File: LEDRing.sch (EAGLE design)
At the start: 35 parts, among them U1 ATMEGA328P-AU, U2 MCP73831, U3 MIC5219 3.3V, U4 MMA8452Q, Y1 16MHZ

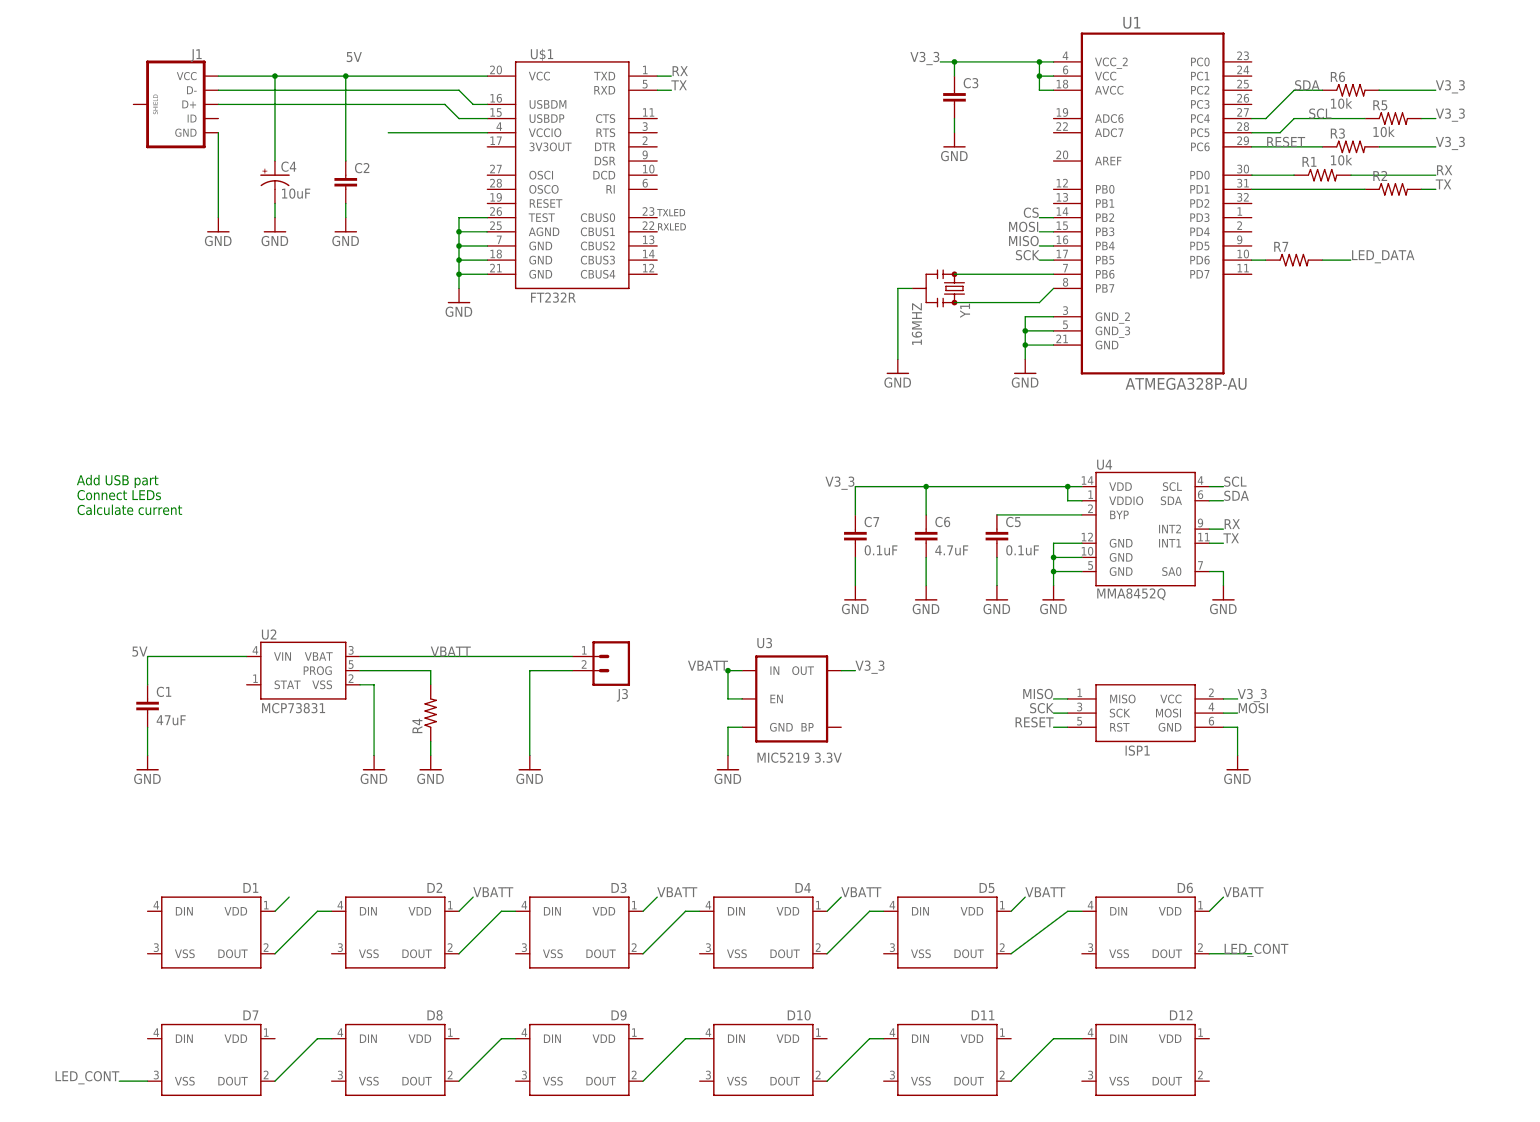
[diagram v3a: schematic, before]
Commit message: Moved USB connector
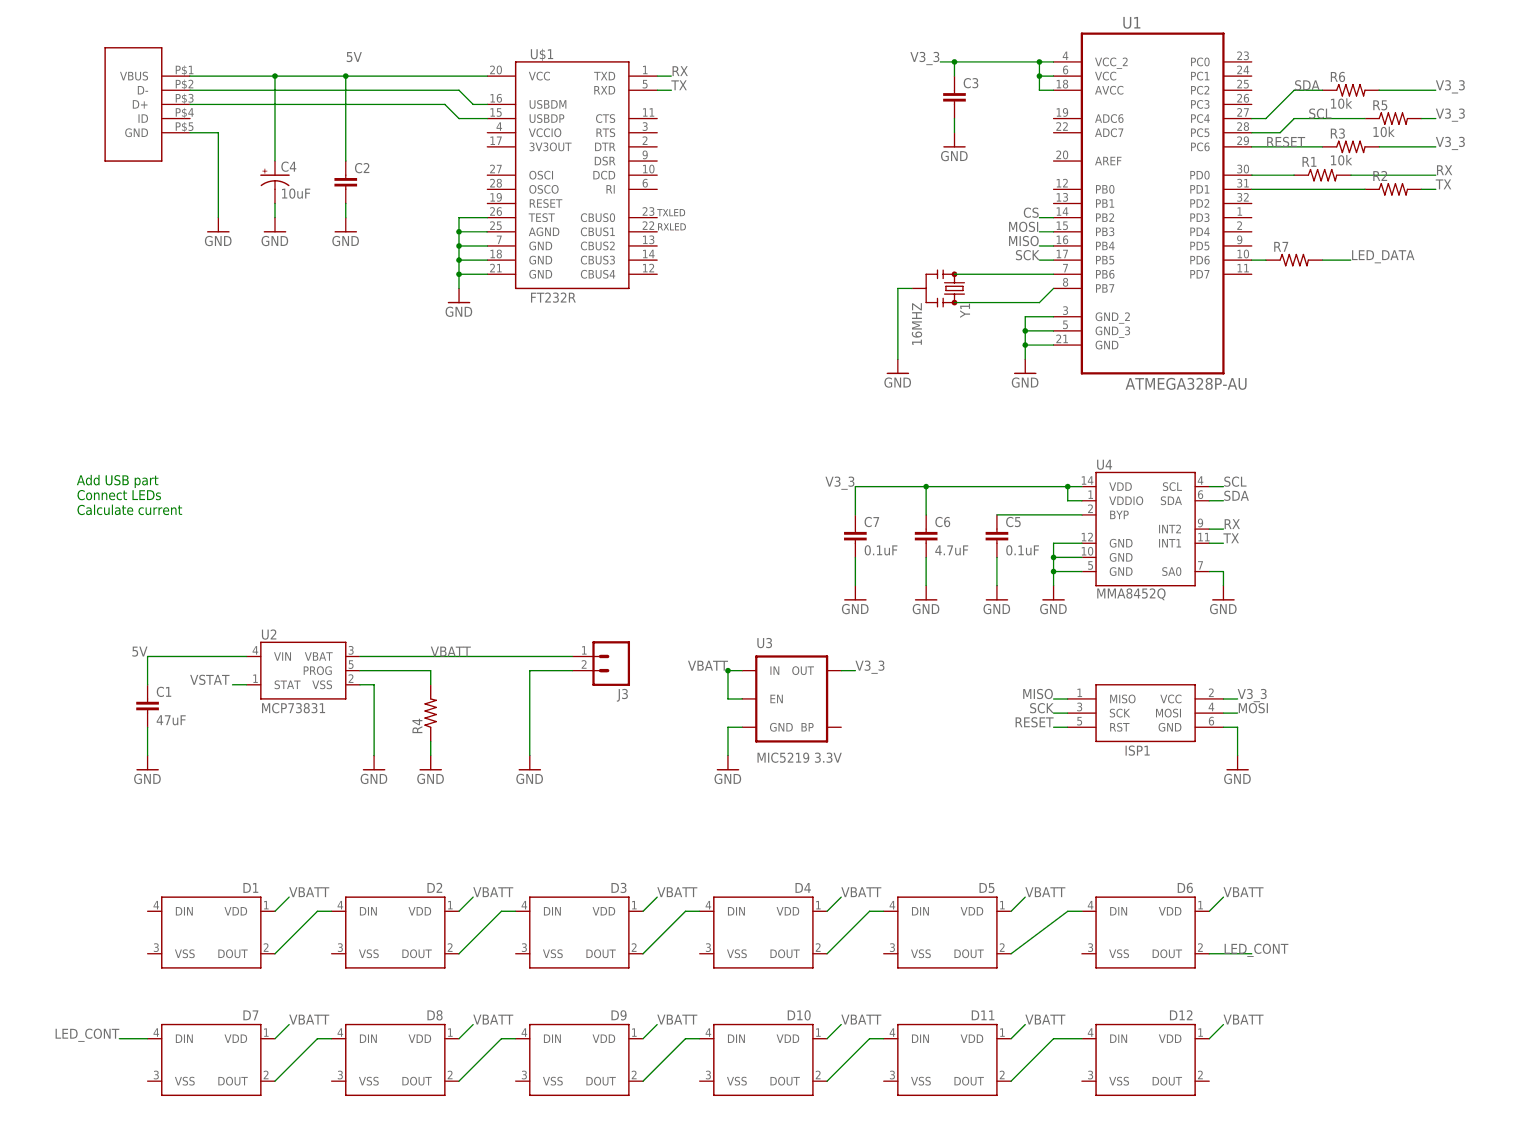
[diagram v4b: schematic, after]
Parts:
- removed J1: (no value), SparkFun-Connectors:USB_MICROB_PLUG-SMT
- added U$2: TE_USB_A121025CT, LEDRingLib:TE_USB_A121025CT
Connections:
- removed net N$6: U$1.VCCIO
- new net VSTAT: U2.STAT
- net 5V: now also U$2.VBUS; no longer J1.VCC
- net GND: now also U$2.GND; no longer J1.GND
- net LED_CONT: now also D7.DIN; no longer D7.VSS
- net N$4: now also U$2.D-; no longer J1.D-
- net N$5: now also U$2.D+; no longer J1.D+
- net VBATT: now also D10.VDD, D11.VDD, D12.VDD, D7.VDD, D8.VDD, D9.VDD
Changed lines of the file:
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@@
 <part name="R2" library="SparkFun-Passives" deviceset="RESISTOR" device="0603-RES"/>
 <part name="U$1" library="GeekAmmo" deviceset="FT232R" device=""/>
-<part name="J1" library="SparkFun-Connectors" deviceset="USB_MICROB_PLUG" device="-SMT"/>
 <part name="GND1" library="SparkFun-Aesthetics" deviceset="GND" device=""/>
 <part name="GND2" library="SparkFun-Aesthetics" deviceset="GND" device=""/>
@@
 <part name="D12" library="SparkFun-LED" deviceset="WS2812B" device=""/>
 <part name="J3" library="SparkFun-Connectors" deviceset="M02" device="PTH"/>
+<part name="U$2" library="LEDRingLib" deviceset="TE_USB_A121025CT" device=""/>
 </parts>
 <sheets>
@@
 <instance part="R2" gate="G$1" x="137.16" y="73.66"/>
 <instance part="U$1" gate="G$1" x="-10.16" y="76.2"/>
-<instance part="J1" gate="G$1" x="-81.28" y="88.9" rot="MR0"/>
 <instance part="GND1" gate="1" x="-73.66" y="66.04"/>
 <instance part="GND2" gate="1" x="-63.5" y="66.04"/>
@@
 <instance part="D12" gate="G$1" x="99.06" y="-83.82" rot="MR0"/>
 <instance part="J3" gate="G$1" x="-2.54" y="-10.16" rot="R180"/>
+<instance part="U$2" gate="G$1" x="-88.9" y="88.9"/>
 </instances>
 <busses>
@@
 <net name="5V" class="0">
 <segment>
-<pinref part="J1" gate="G$1" pin="VCC"/>
 <pinref part="U$1" gate="G$1" pin="VCC"/>
-<wire x1="-73.66" y1="93.98" x2="-63.5" y2="93.98" width="0.1524" layer="91"/>
+<wire x1="-78.74" y1="93.98" x2="-63.5" y2="93.98" width="0.1524" layer="91"/>
 <wire x1="-63.5" y1="93.98" x2="-50.8" y2="93.98" width="0.1524" layer="91"/>
 <wire x1="-50.8" y1="93.98" x2="-25.4" y2="93.98" width="0.1524" layer="91"/>
@@
 <pinref part="C4" gate="G$1" pin="+"/>
 <label x="-50.8" y="96.52" size="1.778" layer="95"/>
+<pinref part="U$2" gate="G$1" pin="VBUS"/>
 </segment>
 <segment>
@@
 <net name="N$4" class="0">
 <segment>
-<pinref part="J1" gate="G$1" pin="D-"/>
-<wire x1="-73.66" y1="91.44" x2="-30.48" y2="91.44" width="0.1524" layer="91"/>
+<wire x1="-78.74" y1="91.44" x2="-30.48" y2="91.44" width="0.1524" layer="91"/>
 <wire x1="-30.48" y1="91.44" x2="-27.94" y2="88.9" width="0.1524" layer="91"/>
 <pinref part="U$1" gate="G$1" pin="USBDM"/>
 <wire x1="-27.94" y1="88.9" x2="-25.4" y2="88.9" width="0.1524" layer="91"/>
+<pinref part="U$2" gate="G$1" pin="D-"/>
 </segment>
 </net>
 <net name="N$5" class="0">
 <segment>
-<pinref part="J1" gate="G$1" pin="D+"/>
-<wire x1="-73.66" y1="88.9" x2="-33.02" y2="88.9" width="0.1524" layer="91"/>
+<wire x1="-78.74" y1="88.9" x2="-33.02" y2="88.9" width="0.1524" layer="91"/>
 <wire x1="-33.02" y1="88.9" x2="-30.48" y2="86.36" width="0.1524" layer="91"/>
 <pinref part="U$1" gate="G$1" pin="USBDP"/>
 <wire x1="-30.48" y1="86.36" x2="-25.4" y2="86.36" width="0.1524" layer="91"/>
+<pinref part="U$2" gate="G$1" pin="D+"/>
 </segment>
 </net>
 <net name="GND" class="0">
 <segment>
-<pinref part="J1" gate="G$1" pin="GND"/>
 <pinref part="GND1" gate="1" pin="GND"/>
 <wire x1="-73.66" y1="83.82" x2="-73.66" y2="68.58" width="0.1524" layer="91"/>
+<pinref part="U$2" gate="G$1" pin="GND"/>
+<wire x1="-78.74" y1="83.82" x2="-73.66" y2="83.82" width="0.1524" layer="91"/>
 </segment>
 <segment>
@@
 </segment>
 </net>
-<net name="N$6" class="0">
-<segment>
-<pinref part="U$1" gate="G$1" pin="VCCIO"/>
-<wire x1="-25.4" y1="83.82" x2="-43.18" y2="83.82" width="0.1524" layer="91"/>
-</segment>
-</net>
 <net name="N$7" class="0">
 <segment>
@@
 <pinref part="D1" gate="G$1" pin="VDD"/>
 <wire x1="-63.5" y1="-55.88" x2="-60.96" y2="-53.34" width="0.1524" layer="91"/>
+<label x="-60.96" y="-53.34" size="1.778" layer="95"/>
 </segment>
 <segment>
@@
 <wire x1="104.14" y1="-55.88" x2="106.68" y2="-53.34" width="0.1524" layer="91"/>
 <label x="106.68" y="-53.34" size="1.778" layer="95"/>
+</segment>
+<segment>
+<pinref part="D7" gate="G$1" pin="VDD"/>
+<wire x1="-63.5" y1="-78.74" x2="-60.96" y2="-76.2" width="0.1524" layer="91"/>
+<label x="-60.96" y="-76.2" size="1.778" layer="95"/>
+</segment>
+<segment>
+<pinref part="D8" gate="G$1" pin="VDD"/>
+<wire x1="-30.48" y1="-78.74" x2="-27.94" y2="-76.2" width="0.1524" layer="91"/>
+<label x="-27.94" y="-76.2" size="1.778" layer="95"/>
+</segment>
+<segment>
+<pinref part="D9" gate="G$1" pin="VDD"/>
+<wire x1="2.54" y1="-78.74" x2="5.08" y2="-76.2" width="0.1524" layer="91"/>
+<label x="5.08" y="-76.2" size="1.778" layer="95"/>
+</segment>
+<segment>
+<pinref part="D10" gate="G$1" pin="VDD"/>
+<wire x1="35.56" y1="-78.74" x2="38.1" y2="-76.2" width="0.1524" layer="91"/>
+<label x="38.1" y="-76.2" size="1.778" layer="95"/>
+</segment>
+<segment>
+<pinref part="D11" gate="G$1" pin="VDD"/>
+<wire x1="68.58" y1="-78.74" x2="71.12" y2="-76.2" width="0.1524" layer="91"/>
+<label x="71.12" y="-76.2" size="1.778" layer="95"/>
+</segment>
+<segment>
+<pinref part="D12" gate="G$1" pin="VDD"/>
+<wire x1="104.14" y1="-78.74" x2="106.68" y2="-76.2" width="0.1524" layer="91"/>
+<label x="106.68" y="-76.2" size="1.778" layer="95"/>
 </segment>
 </net>
@@
 </segment>
 <segment>
-<pinref part="D7" gate="G$1" pin="VSS"/>
-<wire x1="-86.36" y1="-86.36" x2="-91.44" y2="-86.36" width="0.1524" layer="91"/>
-<label x="-91.44" y="-86.36" size="1.778" layer="95" rot="MR0"/>
+<pinref part="D7" gate="G$1" pin="DIN"/>
+<wire x1="-86.36" y1="-78.74" x2="-91.44" y2="-78.74" width="0.1524" layer="91"/>
+<label x="-91.44" y="-78.74" size="1.778" layer="95" rot="MR0"/>
 </segment>
 </net>
@@
 </segment>
 </net>
+<net name="VSTAT" class="0">
+<segment>
+<pinref part="U2" gate="G$1" pin="STAT"/>
+<wire x1="-68.58" y1="-15.24" x2="-71.12" y2="-15.24" width="0.1524" layer="91"/>
+<label x="-78.74" y="-15.24" size="1.778" layer="95"/>
+</segment>
+</net>

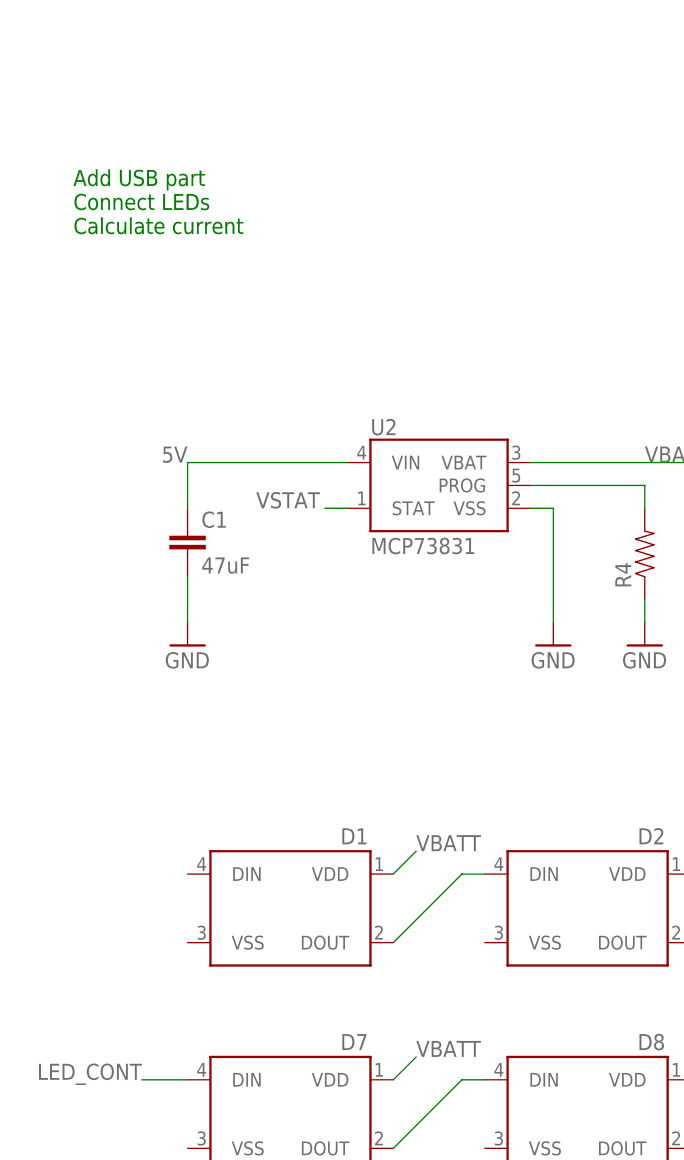
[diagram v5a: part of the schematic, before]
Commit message: Started tieing LED VSS to GND
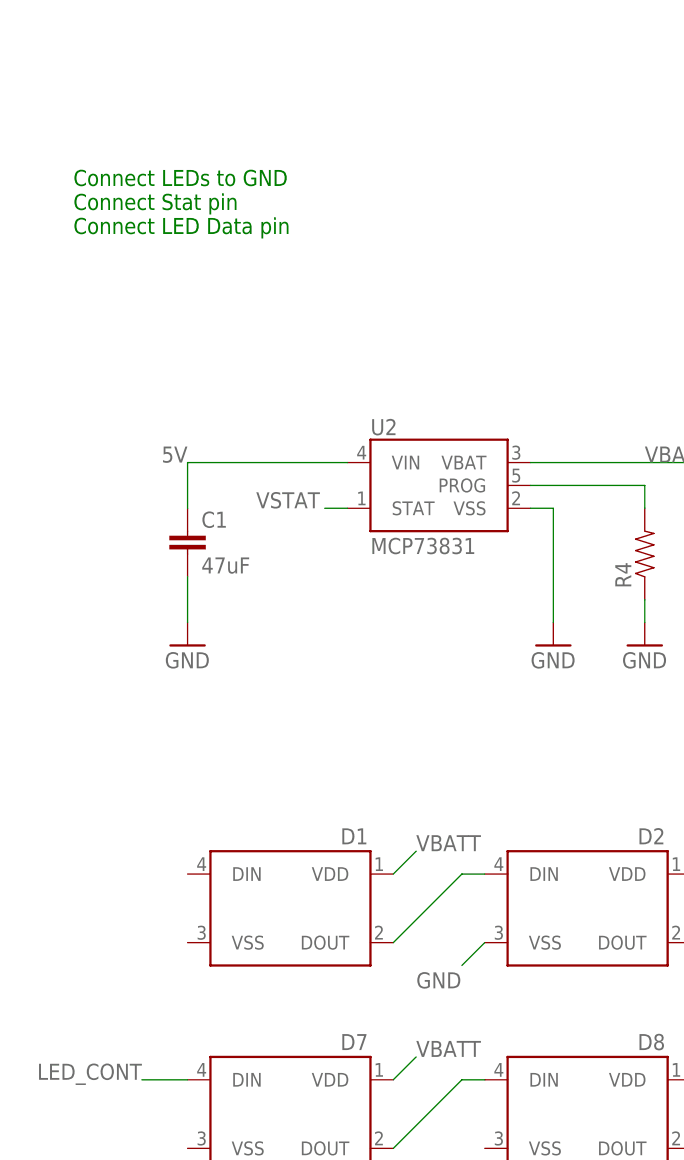
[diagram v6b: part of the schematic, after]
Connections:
- net GND: now also D2.VSS
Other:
- note added: "Connect LEDs to GND Connect Stat pin Connect LED Data pin"
- note removed: "Add USB part Connect LEDs Calculate current"
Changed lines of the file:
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@@
 <sheet>
 <plain>
-<text x="-99.06" y="15.24" size="1.778" layer="91">Add USB part
-Connect LEDs
-Calculate current
-</text>
+<text x="-99.06" y="15.24" size="1.778" layer="91">Connect LEDs to GND
+Connect Stat pin
+Connect LED Data pin</text>
 </plain>
 <instances>
@@
 <wire x1="53.34" y1="7.62" x2="53.34" y2="2.54" width="0.1524" layer="91"/>
 </segment>
-</net>
+<segment>
+<pinref part="D2" gate="G$1" pin="VSS"/>
+<wire x1="-53.34" y1="-63.5" x2="-55.88" y2="-66.04" width="0.1524" layer="91"/>
+<label x="-60.96" y="-68.58" size="1.778" layer="95"/>
+</segment>
+</net>

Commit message: Finished layout. Need to fix text
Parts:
- added R8: (no value), SparkFun-Passives:RESISTOR0603-RES
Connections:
- net 5V: now also R8.2
- net GND: now also D1.VSS, D10.VSS, D11.VSS, D12.VSS, D3.VSS, D4.VSS, D5.VSS, D6.VSS, D7.VSS, D8.VSS, D9.VSS
- net LED_DATA: now also D1.DIN
- net VSTAT: now also R8.1, U1.PD3
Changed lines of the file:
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@@
 <part name="J3" library="SparkFun-Connectors" deviceset="M02" device="PTH"/>
 <part name="U$2" library="LEDRingLib" deviceset="TE_USB_A121025CT" device=""/>
+<part name="R8" library="SparkFun-Passives" deviceset="RESISTOR" device="0603-RES"/>
 </parts>
 <sheets>
@@
 <instance part="J3" gate="G$1" x="-2.54" y="-10.16" rot="R180"/>
 <instance part="U$2" gate="G$1" x="-88.9" y="88.9"/>
+<instance part="R8" gate="G$1" x="-106.68" y="-17.78" rot="R90"/>
 </instances>
 <busses>
@@
 <wire x1="-86.36" y1="-10.16" x2="-68.58" y2="-10.16" width="0.1524" layer="91"/>
 <label x="-86.36" y="-10.16" size="1.778" layer="95" rot="MR0"/>
+</segment>
+<segment>
+<pinref part="R8" gate="G$1" pin="2"/>
+<wire x1="-106.68" y1="-10.16" x2="-106.68" y2="-12.7" width="0.1524" layer="91"/>
+<label x="-109.22" y="-10.16" size="1.778" layer="95"/>
 </segment>
 </net>
@@
 <pinref part="D2" gate="G$1" pin="VSS"/>
 <wire x1="-53.34" y1="-63.5" x2="-55.88" y2="-66.04" width="0.1524" layer="91"/>
-<label x="-60.96" y="-68.58" size="1.778" layer="95"/>
+<label x="-55.88" y="-66.04" size="1.778" layer="95" rot="R180"/>
+</segment>
+<segment>
+<pinref part="D3" gate="G$1" pin="VSS"/>
+<wire x1="-20.32" y1="-63.5" x2="-22.86" y2="-66.04" width="0.1524" layer="91"/>
+<label x="-22.86" y="-66.04" size="1.778" layer="95" rot="R180"/>
+</segment>
+<segment>
+<pinref part="D4" gate="G$1" pin="VSS"/>
+<wire x1="12.7" y1="-63.5" x2="10.16" y2="-66.04" width="0.1524" layer="91"/>
+<label x="10.16" y="-66.04" size="1.778" layer="95" rot="R180"/>
+</segment>
+<segment>
+<pinref part="D5" gate="G$1" pin="VSS"/>
+<wire x1="45.72" y1="-63.5" x2="43.18" y2="-66.04" width="0.1524" layer="91"/>
+<label x="43.18" y="-66.04" size="1.778" layer="95" rot="R180"/>
+</segment>
+<segment>
+<pinref part="D6" gate="G$1" pin="VSS"/>
+<wire x1="81.28" y1="-63.5" x2="78.74" y2="-66.04" width="0.1524" layer="91"/>
+<label x="78.74" y="-66.04" size="1.778" layer="95" rot="R180"/>
+</segment>
+<segment>
+<pinref part="D1" gate="G$1" pin="VSS"/>
+<wire x1="-86.36" y1="-63.5" x2="-88.9" y2="-66.04" width="0.1524" layer="91"/>
+<label x="-88.9" y="-66.04" size="1.778" layer="95" rot="R180"/>
+</segment>
+<segment>
+<pinref part="D7" gate="G$1" pin="VSS"/>
+<wire x1="-86.36" y1="-86.36" x2="-88.9" y2="-88.9" width="0.1524" layer="91"/>
+<label x="-88.9" y="-88.9" size="1.778" layer="95" rot="R180"/>
+</segment>
+<segment>
+<pinref part="D8" gate="G$1" pin="VSS"/>
+<wire x1="-53.34" y1="-86.36" x2="-55.88" y2="-88.9" width="0.1524" layer="91"/>
+<label x="-55.88" y="-88.9" size="1.778" layer="95" rot="R180"/>
+</segment>
+<segment>
+<pinref part="D9" gate="G$1" pin="VSS"/>
+<wire x1="-20.32" y1="-86.36" x2="-22.86" y2="-88.9" width="0.1524" layer="91"/>
+<label x="-22.86" y="-88.9" size="1.778" layer="95" rot="R180"/>
+</segment>
+<segment>
+<pinref part="D10" gate="G$1" pin="VSS"/>
+<wire x1="12.7" y1="-86.36" x2="10.16" y2="-88.9" width="0.1524" layer="91"/>
+<label x="10.16" y="-88.9" size="1.778" layer="95" rot="R180"/>
+</segment>
+<segment>
+<pinref part="D11" gate="G$1" pin="VSS"/>
+<wire x1="45.72" y1="-86.36" x2="43.18" y2="-88.9" width="0.1524" layer="91"/>
+<label x="43.18" y="-88.9" size="1.778" layer="95" rot="R180"/>
+</segment>
+<segment>
+<pinref part="D12" gate="G$1" pin="VSS"/>
+<wire x1="81.28" y1="-86.36" x2="78.74" y2="-88.9" width="0.1524" layer="91"/>
+<label x="78.74" y="-88.9" size="1.778" layer="95" rot="R180"/>
 </segment>
 </net>
@@
 <label x="129.54" y="60.96" size="1.778" layer="95"/>
 </segment>
+<segment>
+<pinref part="D1" gate="G$1" pin="DIN"/>
+<wire x1="-86.36" y1="-55.88" x2="-88.9" y2="-55.88" width="0.1524" layer="91"/>
+<label x="-88.9" y="-55.88" size="1.778" layer="95" rot="MR0"/>
+</segment>
 </net>
 <net name="N$15" class="0">
@@
 <label x="-78.74" y="-15.24" size="1.778" layer="95"/>
 </segment>
-</net>
+<segment>
+<pinref part="U1" gate="A" pin="PD3"/>
+<wire x1="111.76" y1="68.58" x2="114.3" y2="68.58" width="0.1524" layer="91"/>
+<label x="114.3" y="68.58" size="1.778" layer="95"/>
+</segment>
+<segment>
+<pinref part="R8" gate="G$1" pin="1"/>
+<wire x1="-106.68" y1="-22.86" x2="-106.68" y2="-25.4" width="0.1524" layer="91"/>
+<label x="-109.22" y="-27.94" size="1.778" layer="95"/>
+</segment>
+</net>
